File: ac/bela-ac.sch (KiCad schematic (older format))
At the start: 0 parts

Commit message: consolidated schematics etc
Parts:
- added C2, C3: 10uF, Capacitors_ThroughHole:C_Radial_D5_L11_P2, symbol CP
- added C4, C5: 10n, Capacitors_ThroughHole:C_Rect_L4_W2.5_P2.5, symbol C
- added P5: +/-15v, mta-156:MTA-156-4, symbol MTA-156-4
- added P6: 15v_out, Pin_Headers:Pin_Header_Straight_1x02_Pitch2.54mm, symbol CONN_01X02
- added P7: belaaudioout, Pin_Headers:Pin_Header_Straight_1x03_Pitch2.54mm, symbol CONN_01X03
- added P8: belaaudioin, Pin_Headers:Pin_Header_Straight_1x03_Pitch2.54mm, symbol CONN_01X03
- added P9: mod_ac-io, Pin_Headers:Pin_Header_Straight_2x04_Pitch2.54mm, symbol CONN_02X04
- added R10, R9: 10k, xnorman:Resistor_Horizontal_RM10mm-xnorman, symbol R
- added R11, R12, R7, R8: 100k, xnorman:Resistor_Horizontal_RM10mm-xnorman, symbol R
- added R13, R14, R19, R20: 1k, xnorman:Resistor_Horizontal_RM10mm-xnorman, symbol R
- added R15, R16, R17, R18, R5, R6: 2k, xnorman:Resistor_Horizontal_RM10mm-xnorman, symbol R
- added R2, R3: bead, xnorman:Resistor_Vertical_RM5mm-xnor, symbol R
- added U1: TL074, Housings_DIP:DIP-14_W7.62mm_LongPads, symbol TL074
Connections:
- new net: R13.2, R9.1, U1.1
- new net: R5.1, R9.2, U1.2 (-)
- new net: R10.2, R6.1, U1.6 (-)
- new net: R10.1, R14.2, U1.7
- new net: R11.2, R7.1, U1.13 (-)
- new net: R11.1, R15.2, U1.14
- new net: R15.1, R17.2
- new net: R12.1, R16.2, U1.8
- new net: R12.2, R8.1, U1.9 (-)
- new net: R16.1, R18.2
- new net: P5.1 (P1), R2.1
- new net: P5.4 (P4), R3.2
- new net +15v: C2.1, C4.1, P6.1 (P1), R2.2, U1.4 (V+), U1.4 (V+), U1.4 (V+), U1.4 (V+)
- new net -15v: C3.1, C5.2, R3.1, U1.11 (V-), U1.11 (V-), U1.11 (V-), U1.11 (V-)
- new net GND: C2.2, C3.2, C4.2, C5.1, P5.2 (P2), P5.3 (P3), P6.2 (P2), P7.3 (P3), P8.3 (P3), P9.2 (P2), P9.4 (P4), P9.6 (P6), P9.8 (P8), R19.1, R20.1, U1.10 (+), U1.12 (+), U1.3 (+), U1.5 (+)
- new net belaacin1: P8.1 (P1), R17.1, R19.2
- new net belaacin2: P8.2 (P2), R18.1, R20.2
- new net belaacout1: P7.1 (P1), R5.2
- new net belaacout2: P7.2 (P2), R6.2
- new net modularacin1: P9.5 (P5), R7.2
- new net modularacin2: P9.7 (P7), R8.2
- new net modularacout1: P9.1 (P1), R13.1
- new net modularacout2: P9.3 (P3), R14.1
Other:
- note added: "bela out is +/-1V and input expects +/- 1V\nmodular is +/- 5V"
- note added: "decoupling caps"

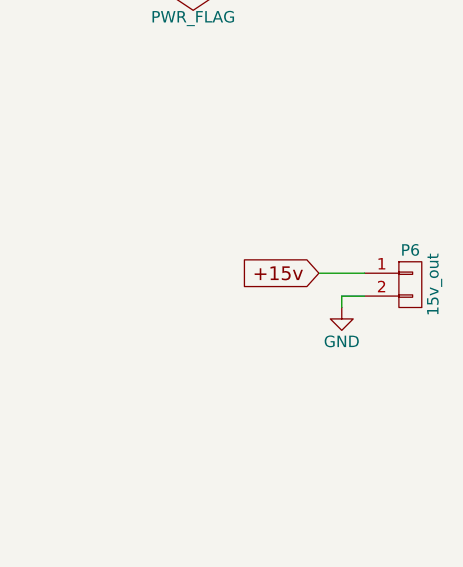
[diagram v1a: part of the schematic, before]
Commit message: removed ac from extra, added power connection for 15
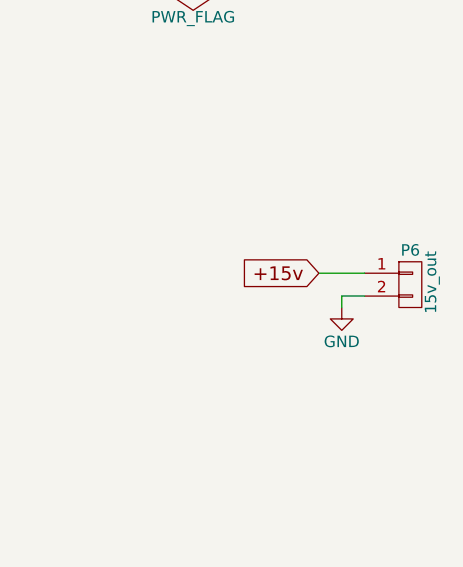
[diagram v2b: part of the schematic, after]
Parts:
- removed P6: 15v_out, Pin_Headers:Pin_Header_Straight_1x02_Pitch2.54mm, symbol CONN_01X02
- added P6: 15v_out, mta-156:MTA-156-2, symbol MTA-156-2
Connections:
- net +15v: now also P6.1 (P1)
- net GND: now also P6.2 (P2)
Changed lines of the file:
@@
 LIBS:valves
 LIBS:xnorman
+LIBS:mta-156
 LIBS:bela-ac-cache
 EELAYER 25 0
@@
 	-1   0    0    1
 $EndComp
-$Comp
-L CONN_01X02 P6
-U 1 1 58726BA3
-P 10300 3550
-F 0 "P6" H 10300 3700 50  0000 C CNN
-F 1 "15v_out" V 10400 3550 50  0000 C CNN
-F 2 "Pin_Headers:Pin_Header_Straight_1x02_Pitch2.54mm" H 10300 3550 50  0001 C CNN
-F 3 "" H 10300 3550 50  0000 C CNN
-	1    10300 3550
-	1    0    0    -1
-$EndComp
 Wire Wire Line
 	9150 1700 9050 1700
@@
 Wire Wire Line
 	10000 3600 10000 3650
+$Comp
+L MTA-156-2 P6
+U 1 1 58727577
+P 10300 3650
+F 0 "P6" H 10300 3900 50  0000 C CNN
+F 1 "15v_out" V 10390 3760 50  0000 C CNN
+F 2 "mta-156:MTA-156-2" H 10300 3650 50  0001 C CNN
+F 3 "" H 10300 3650 50  0000 C CNN
+	1    10300 3650
+	1    0    0    -1
+$EndComp
 $EndSCHEMATC

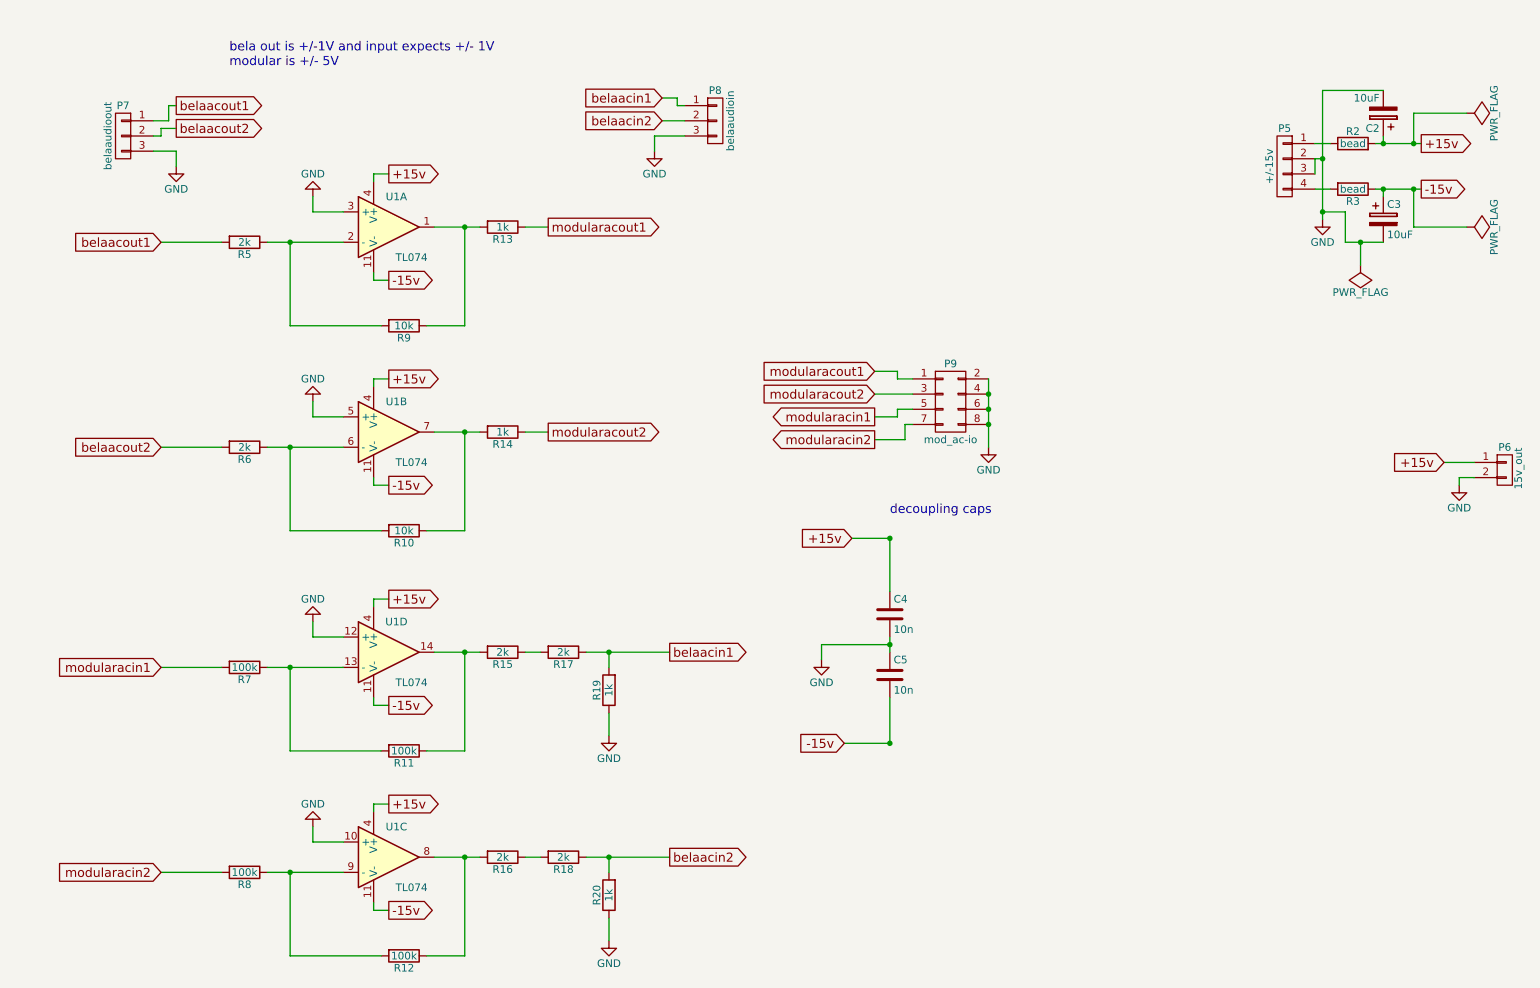
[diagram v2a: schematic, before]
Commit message: added trimmer, removed b.s., almost ready to route
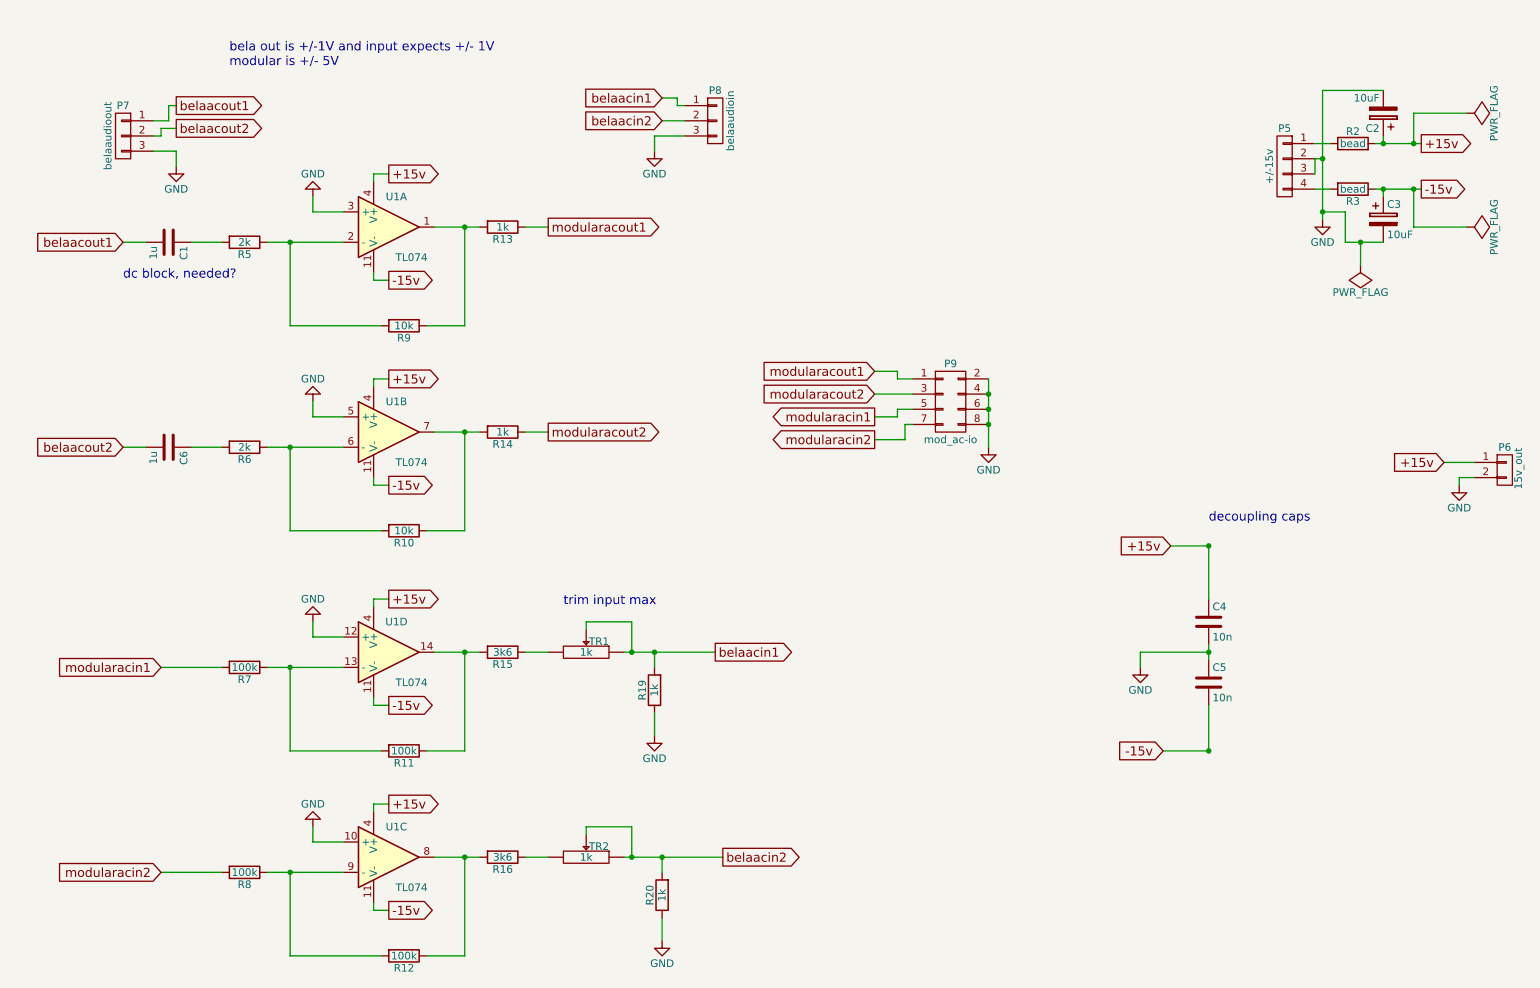
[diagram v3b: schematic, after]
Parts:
- removed R17, R18: 2k, xnorman:Resistor_Horizontal_RM10mm-xnorman, symbol R
- added C1, C6: 1u, Capacitors_ThroughHole:C_Rect_L4_W2.5_P2.5, symbol C
- added TR1, TR2: 1k, trim:trimmer, symbol TRIM
- R15, R16: value 2k -> 3k6
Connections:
- net belaacin1: now also TR1.1, TR1.2
- net belaacin2: now also TR2.1, TR2.2
- net belaacout1: now also C1.2; no longer R5.2
- net belaacout2: now also C6.2; no longer R6.2
- net at R15.1: now also TR1.3
- net at R16.1: now also TR2.3
- new net: C1.1, R5.2
- new net: C6.1, R6.2
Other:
- note added: "dc block, needed?"
- note added: "trim input max"
- moved on the sheet: C4, C5, R19, R20
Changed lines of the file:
@@
 LIBS:xnorman
 LIBS:mta-156
+LIBS:trim
 LIBS:bela-ac-cache
 EELAYER 25 0
@@
 Wire Wire Line
 	2850 1600 2850 1650
-Text GLabel 1450 2050 0    60   Input ~ 0
+Text GLabel 1200 2050 0    60   Input ~ 0
 belaacout1
 Wire Wire Line
-	1850 2050 1450 2050
+	1850 2050 1650 2050
 Text GLabel 4000 1950 2    60   Output ~ 0
 modularacout1
@@
 Wire Wire Line
 	2850 2950 2850 3000
-Text GLabel 1450 3400 0    60   Input ~ 0
+Text GLabel 1200 3400 0    60   Input ~ 0
 belaacout2
 Wire Wire Line
-	1850 3400 1450 3400
+	1850 3400 1650 3400
 Text GLabel 4000 3300 2    60   Output ~ 0
 modularacout2
@@
 Wire Wire Line
 	1850 4850 1450 4850
-Text GLabel 4800 4750 2    60   Output ~ 0
+Text GLabel 5100 4750 2    60   Output ~ 0
 belaacin1
 Connection ~ 3450 4750
@@
 P 3700 4750
 F 0 "R15" V 3780 4750 50  0000 C CNN
-F 1 "2k" V 3700 4750 50  0000 C CNN
+F 1 "3k6" V 3700 4750 50  0000 C CNN
 F 2 "xnorman:Resistor_Horizontal_RM10mm-xnorman" V 3630 4750 50  0001 C CNN
 F 3 "" H 3700 4750 50  0000 C CNN
@@
 $EndComp
 $Comp
-L R R17
-U 1 1 58575412
-P 4100 4750
-F 0 "R17" V 4180 4750 50  0000 C CNN
-F 1 "2k" V 4100 4750 50  0000 C CNN
-F 2 "xnorman:Resistor_Horizontal_RM10mm-xnorman" V 4030 4750 50  0001 C CNN
-F 3 "" H 4100 4750 50  0000 C CNN
-	1    4100 4750
-	0    1    1    0
-$EndComp
-$Comp
 L R R19
 U 1 1 58575419
-P 4400 5000
-F 0 "R19" V 4480 5000 50  0000 C CNN
-F 1 "1k" V 4400 5000 50  0000 C CNN
-F 2 "xnorman:Resistor_Horizontal_RM10mm-xnorman" V 4330 5000 50  0001 C CNN
-F 3 "" H 4400 5000 50  0000 C CNN
-	1    4400 5000
+P 4700 5000
+F 0 "R19" V 4780 5000 50  0000 C CNN
+F 1 "1k" V 4700 5000 50  0000 C CNN
+F 2 "xnorman:Resistor_Horizontal_RM10mm-xnorman" V 4630 5000 50  0001 C CNN
+F 3 "" H 4700 5000 50  0000 C CNN
+	1    4700 5000
 	-1   0    0    1
 $EndComp
 Wire Wire Line
-	3850 4750 3950 4750
-Wire Wire Line
-	4250 4750 4800 4750
-Wire Wire Line
-	4400 4750 4400 4850
-Connection ~ 4400 4750
+	3850 4750 4000 4750
+Wire Wire Line
+	4500 4750 5100 4750
+Wire Wire Line
+	4700 4750 4700 4850
+Connection ~ 4700 4750
 $Comp
 L GND #PWR04
 U 1 1 58575424
-P 4400 5300
-F 0 "#PWR04" H 4400 5050 50  0001 C CNN
-F 1 "GND" H 4400 5150 50  0000 C CNN
-F 2 "" H 4400 5300 50  0000 C CNN
-F 3 "" H 4400 5300 50  0000 C CNN
-	1    4400 5300
-	1    0    0    -1
-$EndComp
-Wire Wire Line
-	4400 5150 4400 5300
+P 4700 5300
+F 0 "#PWR04" H 4700 5050 50  0001 C CNN
+F 1 "GND" H 4700 5150 50  0000 C CNN
+F 2 "" H 4700 5300 50  0000 C CNN
+F 3 "" H 4700 5300 50  0000 C CNN
+	1    4700 5300
+	1    0    0    -1
+$EndComp
+Wire Wire Line
+	4700 5150 4700 5300
 $Comp
 L TL074 U1
@@
 Wire Wire Line
 	1850 6200 1450 6200
-Text GLabel 4800 6100 2    60   Output ~ 0
+Text GLabel 5150 6100 2    60   Output ~ 0
 belaacin2
 Connection ~ 3450 6100
@@
 P 3700 6100
 F 0 "R16" V 3780 6100 50  0000 C CNN
-F 1 "2k" V 3700 6100 50  0000 C CNN
+F 1 "3k6" V 3700 6100 50  0000 C CNN
 F 2 "xnorman:Resistor_Horizontal_RM10mm-xnorman" V 3630 6100 50  0001 C CNN
 F 3 "" H 3700 6100 50  0000 C CNN
@@
 $EndComp
 $Comp
-L R R18
-U 1 1 58575460
-P 4100 6100
-F 0 "R18" V 4180 6100 50  0000 C CNN
-F 1 "2k" V 4100 6100 50  0000 C CNN
-F 2 "xnorman:Resistor_Horizontal_RM10mm-xnorman" V 4030 6100 50  0001 C CNN
-F 3 "" H 4100 6100 50  0000 C CNN
-	1    4100 6100
-	0    1    1    0
-$EndComp
-$Comp
 L R R20
 U 1 1 58575467
-P 4400 6350
-F 0 "R20" V 4480 6350 50  0000 C CNN
-F 1 "1k" V 4400 6350 50  0000 C CNN
-F 2 "xnorman:Resistor_Horizontal_RM10mm-xnorman" V 4330 6350 50  0001 C CNN
-F 3 "" H 4400 6350 50  0000 C CNN
-	1    4400 6350
+P 4750 6350
+F 0 "R20" V 4830 6350 50  0000 C CNN
+F 1 "1k" V 4750 6350 50  0000 C CNN
+F 2 "xnorman:Resistor_Horizontal_RM10mm-xnorman" V 4680 6350 50  0001 C CNN
+F 3 "" H 4750 6350 50  0000 C CNN
+	1    4750 6350
 	-1   0    0    1
 $EndComp
 Wire Wire Line
-	3850 6100 3950 6100
-Wire Wire Line
-	4250 6100 4800 6100
-Wire Wire Line
-	4400 6100 4400 6200
-Connection ~ 4400 6100
+	3850 6100 4000 6100
+Wire Wire Line
+	4500 6100 5150 6100
+Wire Wire Line
+	4750 6100 4750 6200
+Connection ~ 4750 6100
 $Comp
 L GND #PWR06
 U 1 1 58575472
-P 4400 6650
-F 0 "#PWR06" H 4400 6400 50  0001 C CNN
-F 1 "GND" H 4400 6500 50  0000 C CNN
-F 2 "" H 4400 6650 50  0000 C CNN
-F 3 "" H 4400 6650 50  0000 C CNN
-	1    4400 6650
-	1    0    0    -1
-$EndComp
-Wire Wire Line
-	4400 6500 4400 6650
+P 4750 6650
+F 0 "#PWR06" H 4750 6400 50  0001 C CNN
+F 1 "GND" H 4750 6500 50  0000 C CNN
+F 2 "" H 4750 6650 50  0000 C CNN
+F 3 "" H 4750 6650 50  0000 C CNN
+	1    4750 6650
+	1    0    0    -1
+$EndComp
+Wire Wire Line
+	4750 6500 4750 6650
 Text Notes 1900 900  0    60   ~ 0
 bela out is +/-1V and input expects +/- 1V\nmodular is +/- 5V
@@
 L C C4
 U 1 1 5871BD68
-P 6250 4500
-F 0 "C4" H 6275 4600 50  0000 L CNN
-F 1 "10n" H 6275 4400 50  0000 L CNN
-F 2 "Capacitors_ThroughHole:C_Rect_L4_W2.5_P2.5" H 6288 4350 50  0001 C CNN
-F 3 "" H 6250 4500 50  0000 C CNN
-	1    6250 4500
+P 8350 4550
+F 0 "C4" H 8375 4650 50  0000 L CNN
+F 1 "10n" H 8375 4450 50  0000 L CNN
+F 2 "Capacitors_ThroughHole:C_Rect_L4_W2.5_P2.5" H 8388 4400 50  0001 C CNN
+F 3 "" H 8350 4550 50  0000 C CNN
+	1    8350 4550
 	1    0    0    -1
 $EndComp
@@
 L C C5
 U 1 1 5871BD6F
-P 6250 4900
-F 0 "C5" H 6275 5000 50  0000 L CNN
-F 1 "10n" H 6275 4800 50  0000 L CNN
-F 2 "Capacitors_ThroughHole:C_Rect_L4_W2.5_P2.5" H 6288 4750 50  0001 C CNN
-F 3 "" H 6250 4900 50  0000 C CNN
-	1    6250 4900
-	1    0    0    -1
-$EndComp
-Text GLabel 6000 4000 0    60   Input ~ 0
+P 8350 4950
+F 0 "C5" H 8375 5050 50  0000 L CNN
+F 1 "10n" H 8375 4850 50  0000 L CNN
+F 2 "Capacitors_ThroughHole:C_Rect_L4_W2.5_P2.5" H 8388 4800 50  0001 C CNN
+F 3 "" H 8350 4950 50  0000 C CNN
+	1    8350 4950
+	1    0    0    -1
+$EndComp
+Text GLabel 8100 4050 0    60   Input ~ 0
 +15v
-Text GLabel 5950 5350 0    60   Input ~ 0
+Text GLabel 8050 5400 0    60   Input ~ 0
 -15v
 $Comp
 L GND #PWR010
 U 1 1 5871BD94
-P 5800 4800
-F 0 "#PWR010" H 5800 4550 50  0001 C CNN
-F 1 "GND" H 5800 4650 50  0000 C CNN
-F 2 "" H 5800 4800 50  0000 C CNN
-F 3 "" H 5800 4800 50  0000 C CNN
-	1    5800 4800
-	1    0    0    -1
-$EndComp
-Text Notes 6250 3850 0    60   ~ 0
+P 7900 4850
+F 0 "#PWR010" H 7900 4600 50  0001 C CNN
+F 1 "GND" H 7900 4700 50  0000 C CNN
+F 2 "" H 7900 4850 50  0000 C CNN
+F 3 "" H 7900 4850 50  0000 C CNN
+	1    7900 4850
+	1    0    0    -1
+$EndComp
+Text Notes 8350 3900 0    60   ~ 0
 decoupling caps
 Wire Wire Line
-	6250 4650 6250 4750
-Connection ~ 6250 4700
-Wire Wire Line
-	6250 4000 6250 4350
-Wire Wire Line
-	6250 5050 6250 5350
-Wire Wire Line
-	5800 4800 5800 4700
-Connection ~ 6250 5350
-Connection ~ 6250 4000
-Wire Wire Line
-	6250 4000 6000 4000
-Wire Wire Line
-	5800 4700 6250 4700
-Wire Wire Line
-	6250 5350 5950 5350
+	8350 4700 8350 4800
+Connection ~ 8350 4750
+Wire Wire Line
+	8350 4050 8350 4400
+Wire Wire Line
+	8350 5100 8350 5400
+Wire Wire Line
+	7900 4850 7900 4750
+Connection ~ 8350 5400
+Connection ~ 8350 4050
+Wire Wire Line
+	8350 4050 8100 4050
+Wire Wire Line
+	7900 4750 8350 4750
+Wire Wire Line
+	8350 5400 8050 5400
 $Comp
 L R R2
@@
 	1    0    0    -1
 $EndComp
+$Comp
+L C C1
+U 1 1 58727AF1
+P 1500 2050
+F 0 "C1" H 1525 2150 50  0000 L CNN
+F 1 "1u" H 1525 1950 50  0000 L CNN
+F 2 "Capacitors_ThroughHole:C_Rect_L4_W2.5_P2.5" H 1538 1900 50  0001 C CNN
+F 3 "" H 1500 2050 50  0000 C CNN
+	1    1500 2050
+	0    1    1    0
+$EndComp
+$Comp
+L C C6
+U 1 1 58727B9F
+P 1500 3400
+F 0 "C6" H 1525 3500 50  0000 L CNN
+F 1 "1u" H 1525 3300 50  0000 L CNN
+F 2 "Capacitors_ThroughHole:C_Rect_L4_W2.5_P2.5" H 1538 3250 50  0001 C CNN
+F 3 "" H 1500 3400 50  0000 C CNN
+	1    1500 3400
+	0    1    1    0
+$EndComp
+$Comp
+L TRIM TR2
+U 1 1 58728084
+P 4250 6100
+F 0 "TR2" V 4150 6184 50  0000 C TNN
+F 1 "1k" V 4250 6100 50  0000 C CNN
+F 2 "trim:trimmer" H 4250 6100 50  0001 C CNN
+F 3 "" H 4250 6100 50  0000 C CNN
+	1    4250 6100
+	0    1    1    0
+$EndComp
+$Comp
+L TRIM TR1
+U 1 1 587283B7
+P 4250 4750
+F 0 "TR1" V 4150 4834 50  0000 C TNN
+F 1 "1k" V 4250 4750 50  0000 C CNN
+F 2 "trim:trimmer" H 4250 4750 50  0001 C CNN
+F 3 "" H 4250 4750 50  0000 C CNN
+	1    4250 4750
+	0    1    1    0
+$EndComp
+Wire Wire Line
+	4250 5950 4250 5900
+Wire Wire Line
+	4250 5900 4550 5900
+Wire Wire Line
+	4550 5900 4550 6100
+Connection ~ 4550 6100
+Wire Wire Line
+	4250 4600 4250 4550
+Wire Wire Line
+	4250 4550 4550 4550
+Wire Wire Line
+	4550 4550 4550 4750
+Connection ~ 4550 4750
+Text Notes 4100 4450 0    60   ~ 0
+trim input max
+Wire Wire Line
+	1350 3400 1200 3400
+Wire Wire Line
+	1350 2050 1200 2050
+Text Notes 1200 2300 0    60   ~ 0
+dc block, needed?
 $EndSCHEMATC
